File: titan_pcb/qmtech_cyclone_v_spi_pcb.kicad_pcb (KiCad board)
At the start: 2 copper layers, 146.1 x 95 mm, 44 parts, among them J1 FPGA, J10 OLED_CONN, J11 OLED_CONN, J12 CH341_PRG_CONN, J13 SPI_HEADER, J14 SPI_HEADER, J15 I2C_PULLUP, J16 I2C_PULLUP, J17 I2C_PULLUP, J18 I2C_PULLUP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

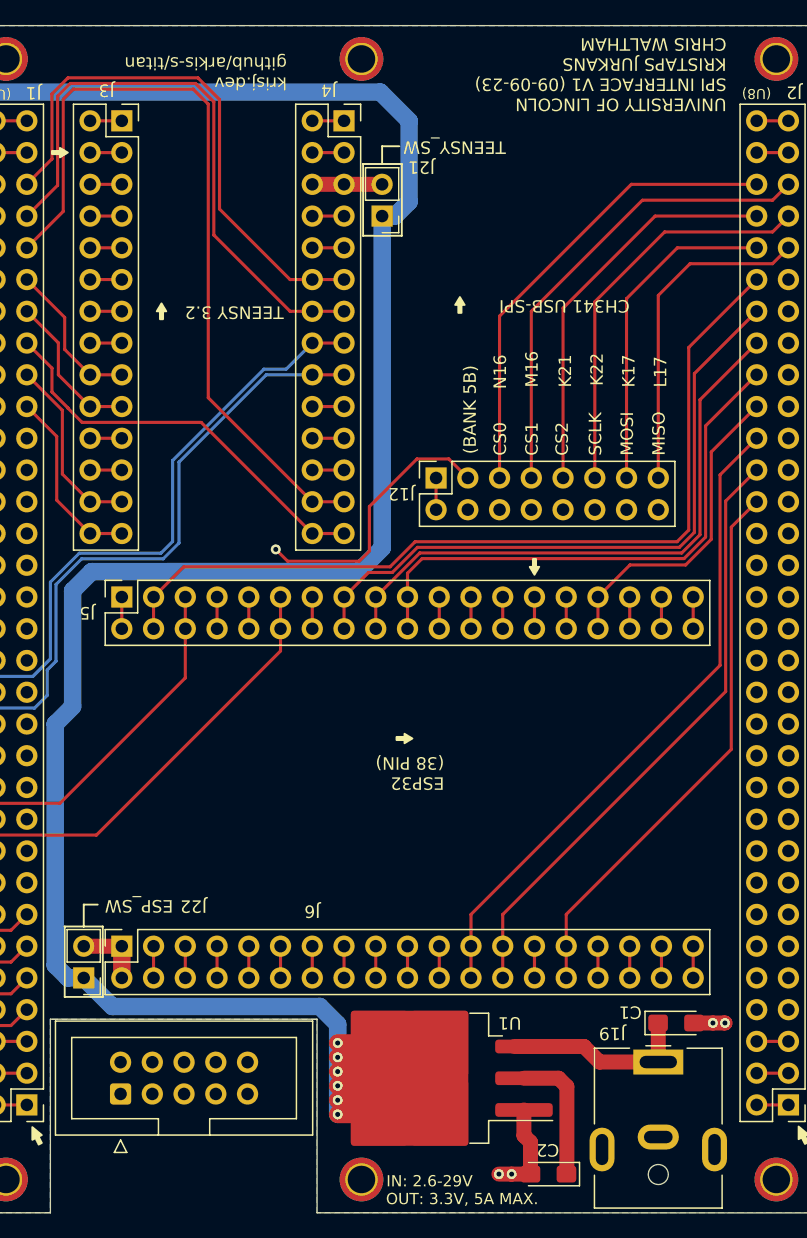
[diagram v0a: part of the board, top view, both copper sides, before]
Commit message: updated silkscreen, added center-positive symbol for power supply
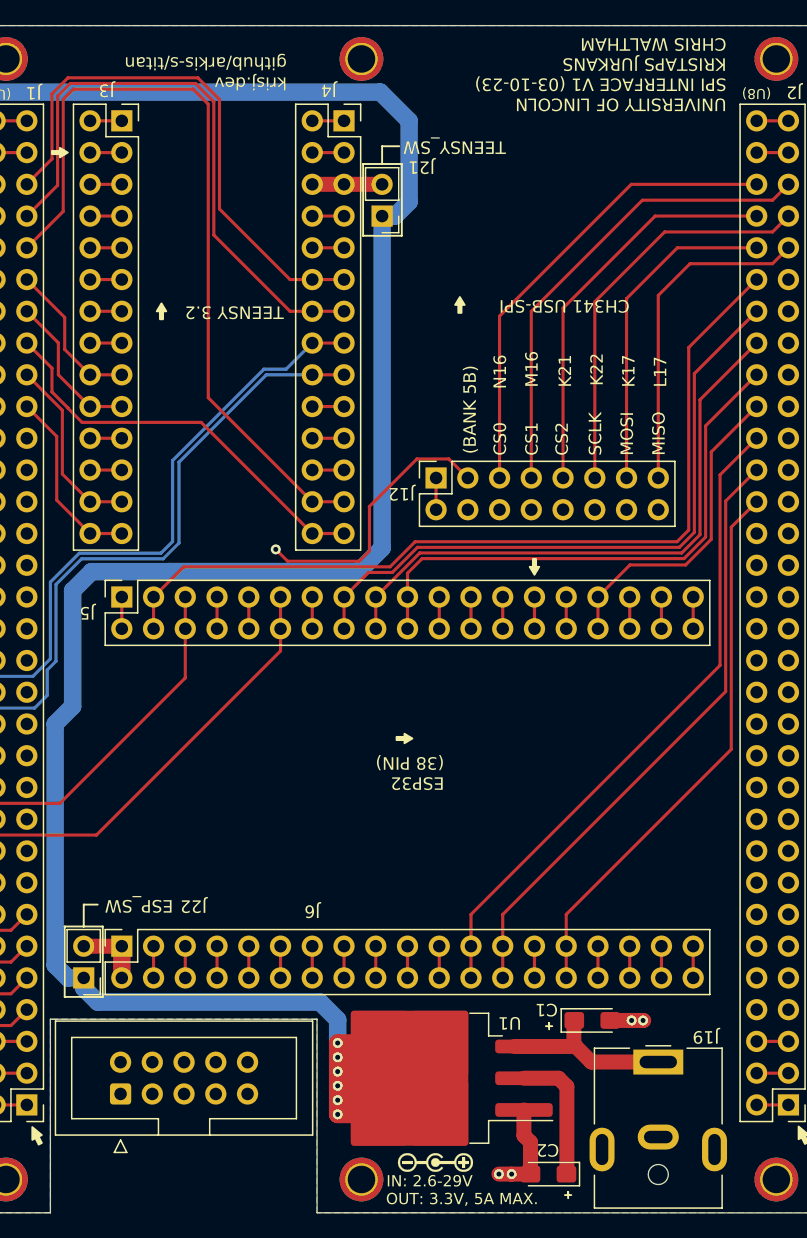
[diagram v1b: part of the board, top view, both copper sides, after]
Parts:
- moved C1 6.71 mm to (134.2, 110.1)
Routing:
- net 3V3: track 369.7 -> 370.4 mm
- net Net-(U1-VI): track 15.2 -> 14.5 mm
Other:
- board text added: "UNIVERSITY OF LINCOLN SPI INTERFACE V1 (03-10-23) KRISTAPS JURKANS CHRIS WALTHAM"
- board text removed: "UNIVERSITY OF LINCOLN SPI INTERFACE V1 (09-09-23) KRISTAPS JURKANS CHRIS WALTHAM"

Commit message: updated pcb
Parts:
- added REF**: TestPoint_Pad_D1.0mm, TestPoint:TestPoint_Pad_D1.0mm, F.Cu at (140.1, 116.2)
- added REF**: TestPoint_Pad_D1.0mm, TestPoint:TestPoint_Pad_D1.0mm, F.Cu at (136.8, 119.7)
- added REF**: TestPoint_Pad_D1.0mm, TestPoint:TestPoint_Pad_D1.0mm, F.Cu at (47.6, 48.7)
- added SW1: PICO_RESET_SW, Button_Switch_THT:SW_PUSH_6mm_H5mm, F.Cu at (119.9, 116.5)
- moved H5 143.5 mm to (39.2, 125.7), turned to 180 degrees
- moved H6 139.8 mm to (39.2, 36.0), turned to 180 degrees
- moved J2 134.4 mm to (38.3, 42.0), turned to 0 degrees
- moved H1 130.6 mm to (140.1, 125.7), turned to 180 degrees
- moved H2 126.6 mm to (140.1, 36.0), turned to 180 degrees
- moved J19 113.4 mm to (48.7, 45.4), turned to 180 degrees
- moved C2 112.9 mm to (57.5, 36.5), turned to 0 degrees
- moved J18 109.6 mm to (137.3, 45.8), turned to 0 degrees
- moved J7 109.1 mm to (129.7, 120.7), turned to 180 degrees
- moved J13 104.7 mm to (124.6, 36.9), turned to 90 degrees
- moved H7 102.2 mm to (72.4, 125.7), turned to 180 degrees
- moved C1 100.9 mm to (54.0, 48.8), turned to 180 degrees
- moved H8 97.0 mm to (72.4, 36.0), turned to 180 degrees
- moved J20 95.1 mm to (109.4, 124.4), turned to 90 degrees
- moved J17 95.0 mm to (137.3, 59.8), turned to 0 degrees
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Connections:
- R1 pad 1: Net-(J15-Pin_4) -> Net-(J18-Pin_3)
- R2 pad 1: Net-(J15-Pin_3) -> Net-(J18-Pin_4)
- R3 pad 1: Net-(J16-Pin_4) -> Net-(J17-Pin_3)
- R4 pad 1: Net-(J16-Pin_3) -> Net-(J17-Pin_4)
- R5 pad 1: Net-(J17-Pin_4) -> Net-(J16-Pin_3)
- R6 pad 1: Net-(J17-Pin_3) -> Net-(J16-Pin_4)
- R7 pad 1: Net-(J18-Pin_4) -> Net-(J15-Pin_3)
- R8 pad 1: Net-(J18-Pin_3) -> Net-(J15-Pin_4)
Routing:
- net PICO_RUN: track 2.54 -> 35.1 mm
- net Net-(U1-VI): track 14.5 -> 17.8 mm
- net 3V3: track 370.4 -> 372.9 mm, vias 10 -> 11
- net GND: track 91.2 -> 93.2 mm, vias 6 -> 7
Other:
- board size 146.1 x 95 mm -> 137.4 x 95 mm
- board text added: "PWR"
- board text added: "UNIVERSITY OF LINCOLN SPI INTERFACE V1 (18-10-23) KRISTAPS JURKANS CHARLES FOX CHRIS WALTHAM"
- board text added: "krisj.dev gh/titan-compiler-project"
- board text removed: "UNIVERSITY OF LINCOLN SPI INTERFACE V1 (03-10-23) KRISTAPS JURKANS CHRIS WALTHAM"
- board text removed: "krisj.dev github/arkis-s/titan"
